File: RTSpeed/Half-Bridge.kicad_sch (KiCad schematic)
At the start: 8 parts, among them Q1 IRF1310, Q2 IRF1310, U1 IR2101

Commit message: Added STM32F411 development schematic
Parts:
- renumbered C2 to C1, C1 to C2, R2 to R1, R1 to R2
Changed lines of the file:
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@@
   (symbol (lib_id "power:GND") (at 48.26 79.375 0) (unit 1)
     (in_bom yes) (on_board yes) (dnp no)
-    (property "Reference" "#PWR03" (at 48.26 85.725 0)
+    (property "Reference" "#PWR02" (at 48.26 85.725 0)
       (effects (font (size 1.27 1.27)) hide)
     )
@@
     (instances
       (project "RTSpeed"
-        (path "/fc8dd9a9-f99a-4338-8182-2c8b4b8ed6dd"
-          (reference "#PWR03") (unit 1)
-        )
         (path "/fc8dd9a9-f99a-4338-8182-2c8b4b8ed6dd/b5458e57-2ddd-4d30-9620-d640c1a391c8"
           (reference "#PWR02") (unit 1)
@@
   (symbol (lib_id "Device:R_US") (at 85.09 95.885 90) (unit 1)
     (in_bom yes) (on_board yes) (dnp no)
-    (property "Reference" "R1" (at 85.09 90.805 90)
+    (property "Reference" "R2" (at 85.09 90.805 90)
       (effects (font (size 1.27 1.27)))
     )
@@
     (instances
       (project "RTSpeed"
-        (path "/fc8dd9a9-f99a-4338-8182-2c8b4b8ed6dd"
-          (reference "R1") (unit 1)
-        )
         (path "/fc8dd9a9-f99a-4338-8182-2c8b4b8ed6dd/b5458e57-2ddd-4d30-9620-d640c1a391c8"
           (reference "R2") (unit 1)
@@
     (instances
       (project "RTSpeed"
-        (path "/fc8dd9a9-f99a-4338-8182-2c8b4b8ed6dd"
-          (reference "Q1") (unit 1)
-        )
         (path "/fc8dd9a9-f99a-4338-8182-2c8b4b8ed6dd/b5458e57-2ddd-4d30-9620-d640c1a391c8"
           (reference "Q1") (unit 1)
@@
     (instances
       (project "RTSpeed"
-        (path "/fc8dd9a9-f99a-4338-8182-2c8b4b8ed6dd"
-          (reference "D1") (unit 1)
-        )
         (path "/fc8dd9a9-f99a-4338-8182-2c8b4b8ed6dd/b5458e57-2ddd-4d30-9620-d640c1a391c8"
           (reference "D1") (unit 1)
@@
     (instances
       (project "RTSpeed"
-        (path "/fc8dd9a9-f99a-4338-8182-2c8b4b8ed6dd"
+        (path "/fc8dd9a9-f99a-4338-8182-2c8b4b8ed6dd/b5458e57-2ddd-4d30-9620-d640c1a391c8"
           (reference "U1") (unit 1)
         )
-        (path "/fc8dd9a9-f99a-4338-8182-2c8b4b8ed6dd/b5458e57-2ddd-4d30-9620-d640c1a391c8"
-          (reference "U1") (unit 1)
-        )
         (path "/fc8dd9a9-f99a-4338-8182-2c8b4b8ed6dd/f8c306d8-017c-4a71-a4b7-a44622ec1e7a"
           (reference "U2") (unit 1)
@@
   (symbol (lib_id "power:GND") (at 96.52 100.965 0) (unit 1)
     (in_bom yes) (on_board yes) (dnp no)
-    (property "Reference" "#PWR02" (at 96.52 107.315 0)
+    (property "Reference" "#PWR04" (at 96.52 107.315 0)
       (effects (font (size 1.27 1.27)) hide)
     )
@@
     (instances
       (project "RTSpeed"
-        (path "/fc8dd9a9-f99a-4338-8182-2c8b4b8ed6dd"
-          (reference "#PWR02") (unit 1)
-        )
         (path "/fc8dd9a9-f99a-4338-8182-2c8b4b8ed6dd/b5458e57-2ddd-4d30-9620-d640c1a391c8"
           (reference "#PWR04") (unit 1)
@@
   (symbol (lib_id "Device:R_US") (at 85.09 83.185 90) (unit 1)
     (in_bom yes) (on_board yes) (dnp no)
-    (property "Reference" "R2" (at 85.09 78.105 90)
+    (property "Reference" "R1" (at 85.09 78.105 90)
       (effects (font (size 1.27 1.27)))
     )
@@
     (instances
       (project "RTSpeed"
-        (path "/fc8dd9a9-f99a-4338-8182-2c8b4b8ed6dd"
-          (reference "R2") (unit 1)
-        )
         (path "/fc8dd9a9-f99a-4338-8182-2c8b4b8ed6dd/b5458e57-2ddd-4d30-9620-d640c1a391c8"
           (reference "R1") (unit 1)
@@
   (symbol (lib_id "Device:C") (at 48.26 75.565 0) (unit 1)
     (in_bom yes) (on_board yes) (dnp no) (fields_autoplaced)
-    (property "Reference" "C2" (at 52.07 74.2949 0)
+    (property "Reference" "C1" (at 52.07 74.2949 0)
       (effects (font (size 1.27 1.27)) (justify left))
     )
@@
     (instances
       (project "RTSpeed"
-        (path "/fc8dd9a9-f99a-4338-8182-2c8b4b8ed6dd"
-          (reference "C2") (unit 1)
-        )
         (path "/fc8dd9a9-f99a-4338-8182-2c8b4b8ed6dd/b5458e57-2ddd-4d30-9620-d640c1a391c8"
           (reference "C1") (unit 1)
@@
     (instances
       (project "RTSpeed"
-        (path "/fc8dd9a9-f99a-4338-8182-2c8b4b8ed6dd"
+        (path "/fc8dd9a9-f99a-4338-8182-2c8b4b8ed6dd/b5458e57-2ddd-4d30-9620-d640c1a391c8"
           (reference "Q2") (unit 1)
         )
-        (path "/fc8dd9a9-f99a-4338-8182-2c8b4b8ed6dd/b5458e57-2ddd-4d30-9620-d640c1a391c8"
-          (reference "Q2") (unit 1)
-        )
         (path "/fc8dd9a9-f99a-4338-8182-2c8b4b8ed6dd/f8c306d8-017c-4a71-a4b7-a44622ec1e7a"
           (reference "Q4") (unit 1)
@@
   (symbol (lib_id "power:GND") (at 62.23 100.965 0) (unit 1)
     (in_bom yes) (on_board yes) (dnp no)
-    (property "Reference" "#PWR04" (at 62.23 107.315 0)
+    (property "Reference" "#PWR03" (at 62.23 107.315 0)
       (effects (font (size 1.27 1.27)) hide)
     )
@@
     (instances
       (project "RTSpeed"
-        (path "/fc8dd9a9-f99a-4338-8182-2c8b4b8ed6dd"
-          (reference "#PWR04") (unit 1)
-        )
         (path "/fc8dd9a9-f99a-4338-8182-2c8b4b8ed6dd/b5458e57-2ddd-4d30-9620-d640c1a391c8"
           (reference "#PWR03") (unit 1)
@@
   (symbol (lib_id "Device:C_Polarized_US") (at 73.025 88.265 0) (unit 1)
     (in_bom yes) (on_board yes) (dnp no)
-    (property "Reference" "C1" (at 76.2 86.995 0)
+    (property "Reference" "C2" (at 76.2 86.995 0)
       (effects (font (size 1.27 1.27)) (justify left))
     )
@@
     (instances
       (project "RTSpeed"
-        (path "/fc8dd9a9-f99a-4338-8182-2c8b4b8ed6dd"
-          (reference "C1") (unit 1)
-        )
         (path "/fc8dd9a9-f99a-4338-8182-2c8b4b8ed6dd/b5458e57-2ddd-4d30-9620-d640c1a391c8"
           (reference "C2") (unit 1)
@@
     (instances
       (project "RTSpeed"
-        (path "/fc8dd9a9-f99a-4338-8182-2c8b4b8ed6dd"
+        (path "/fc8dd9a9-f99a-4338-8182-2c8b4b8ed6dd/b5458e57-2ddd-4d30-9620-d640c1a391c8"
           (reference "#PWR01") (unit 1)
-        )
-        (path "/fc8dd9a9-f99a-4338-8182-2c8b4b8ed6dd/b5458e57-2ddd-4d30-9620-d640c1a391c8"
-          (reference "#PWR01") (unit 1)

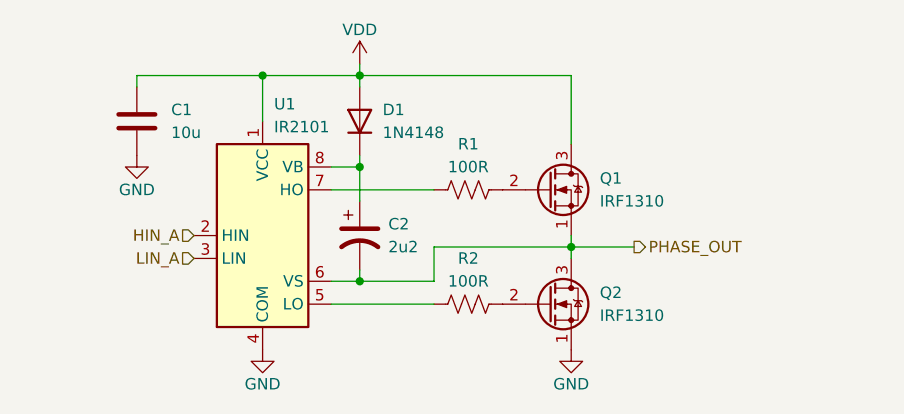
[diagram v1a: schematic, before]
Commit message: Connected Inverter
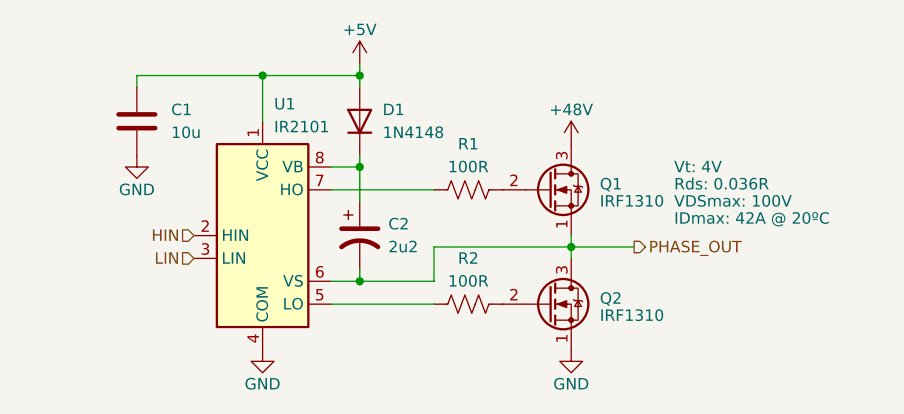
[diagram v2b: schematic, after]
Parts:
- Q1: IDmax (none) -> 42A @ 20ºC; Rds (none) -> 0.036R; VDSmax (none) -> 100V; Vt (none) -> 4V
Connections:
- net HIN_A renamed HIN
- net LIN_A renamed LIN
- net VDD renamed +5V
- net +5V: no longer Q1.3 (D)
- new net +48V: Q1.3 (D)
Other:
- title: (none) -> Half Bridge

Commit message: updated inverter model
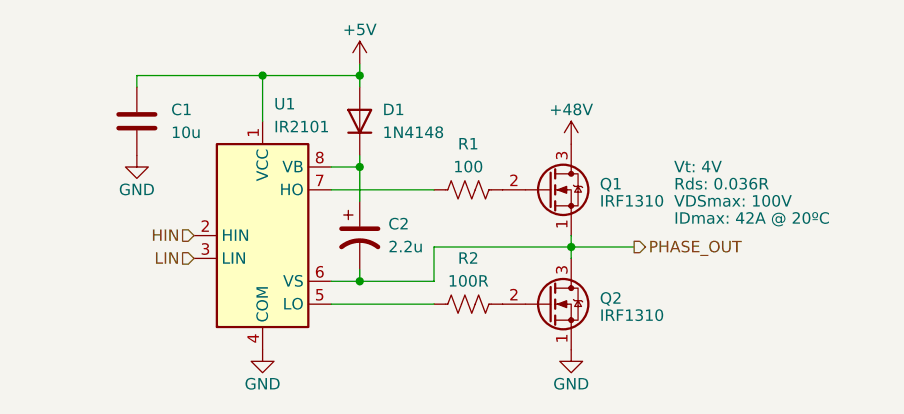
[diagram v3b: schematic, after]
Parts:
- C2: value 2u2 -> 2.2u
- R1: value 100R -> 100
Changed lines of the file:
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@@
       (effects (font (size 1.27 1.27)) (justify left))
+    )
+    (property "Sim.Library" "D:\\dev\\RTSpeed\\simulation\\models\\irf1310ns.spi" (at 93.98 83.185 0)
+      (effects (font (size 1.27 1.27)) hide)
+    )
+    (property "Sim.Name" "irf1310ns" (at 93.98 83.185 0)
+      (effects (font (size 1.27 1.27)) hide)
+    )
+    (property "Sim.Device" "SUBCKT" (at 93.98 83.185 0)
+      (effects (font (size 1.27 1.27)) hide)
+    )
+    (property "Sim.Pins" "1=1 2=2 3=3" (at 93.98 83.185 0)
+      (effects (font (size 1.27 1.27)) hide)
     )
     (pin "1")
@@
       (effects (font (size 1.27 1.27)) hide)
     )
-    (property "Sim.Device" "D" (at 73.025 75.565 0)
-      (effects (font (size 1.27 1.27)) hide)
-    )
-    (property "Sim.Pins" "1=K 2=A" (at 73.025 75.565 0)
+    (property "Sim.Device" "SUBCKT" (at 73.025 75.565 0)
+      (effects (font (size 1.27 1.27)) hide)
+    )
+    (property "Sim.Pins" "1=1 2=2" (at 73.025 75.565 0)
+      (effects (font (size 1.27 1.27)) hide)
+    )
+    (property "Sim.Library" "D:\\dev\\RTSpeed\\simulation\\models\\1N4148.lib" (at 73.025 75.565 0)
+      (effects (font (size 1.27 1.27)) hide)
+    )
+    (property "Sim.Name" "1N4148" (at 73.025 75.565 0)
       (effects (font (size 1.27 1.27)) hide)
     )
@@
     )
     (property "Datasheet" "https://www.infineon.com/dgdl/ir2101.pdf?fileId=5546d462533600a4015355c7a755166c" (at 62.23 88.265 0)
+      (effects (font (size 1.27 1.27)) hide)
+    )
+    (property "Sim.Library" "D:\\dev\\RTSpeed\\simulation\\models\\IR2101.lib" (at 62.23 88.265 0)
+      (effects (font (size 1.27 1.27)) hide)
+    )
+    (property "Sim.Name" "IR2101" (at 62.23 88.265 0)
+      (effects (font (size 1.27 1.27)) hide)
+    )
+    (property "Sim.Device" "SUBCKT" (at 62.23 88.265 0)
+      (effects (font (size 1.27 1.27)) hide)
+    )
+    (property "Sim.Pins" "1=VCC 2=HIN 3=LIN 4=COM 5=LO 6=VS 7=HO 8=VB" (at 62.23 88.265 0)
       (effects (font (size 1.27 1.27)) hide)
     )
@@
       (effects (font (size 1.27 1.27)))
     )
-    (property "Value" "100R" (at 85.09 80.645 90)
+    (property "Value" "100" (at 85.09 80.645 90)
       (effects (font (size 1.27 1.27)))
     )
@@
     )
     (property "Datasheet" "~" (at 85.09 83.185 0)
+      (effects (font (size 1.27 1.27)) hide)
+    )
+    (property "Sim.Device" "R" (at 85.09 83.185 0)
+      (effects (font (size 1.27 1.27)) hide)
+    )
+    (property "Sim.Pins" "1=+ 2=-" (at 85.09 83.185 0)
       (effects (font (size 1.27 1.27)) hide)
     )
@@
       (effects (font (size 1.27 1.27)) (justify left) hide)
     )
+    (property "Sim.Library" "D:\\dev\\RTSpeed\\simulation\\models\\irf1310ns.spi" (at 93.98 95.885 0)
+      (effects (font (size 1.27 1.27)) hide)
+    )
+    (property "Sim.Name" "irf1310ns" (at 93.98 95.885 0)
+      (effects (font (size 1.27 1.27)) hide)
+    )
+    (property "Sim.Device" "SUBCKT" (at 93.98 95.885 0)
+      (effects (font (size 1.27 1.27)) hide)
+    )
+    (property "Sim.Pins" "1=1 2=2 3=3" (at 93.98 95.885 0)
+      (effects (font (size 1.27 1.27)) hide)
+    )
     (pin "1")
     (pin "2")
@@
       (effects (font (size 1.27 1.27)) (justify left))
     )
-    (property "Value" "2u2" (at 76.2 89.535 0)
+    (property "Value" "2.2u" (at 76.2 89.535 0)
       (effects (font (size 1.27 1.27)) (justify left))
     )
@@
       (effects (font (size 1.27 1.27)) hide)
     )
+    (property "Sim.Device" "C" (at 73.025 88.265 0)
+      (effects (font (size 1.27 1.27)) hide)
+    )
+    (property "Sim.Pins" "1=+ 2=-" (at 73.025 88.265 0)
+      (effects (font (size 1.27 1.27)) hide)
+    )

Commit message: Added some footprints
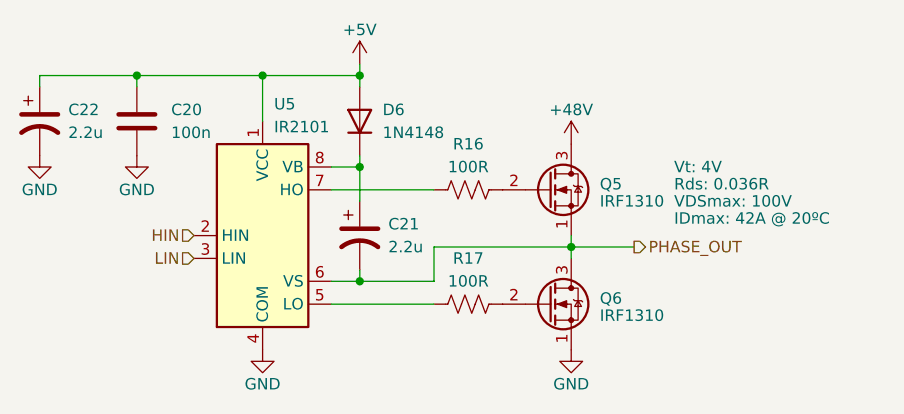
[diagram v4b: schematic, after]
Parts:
- added C22: 2.2u, Capacitor_THT:CP_Radial_D5.0mm_P2.00mm, symbol Device:C_Polarized_US
- C20: renamed from C1; value 10u -> 100n; footprint (none) -> Capacitor_SMD:C_0603_1608Metric
- C21: renamed from C2; footprint (none) -> Capacitor_THT:CP_Radial_D5.0mm_P2.00mm
- D6: renamed from D1; footprint (none) -> Diode_SMD:D_SOD-123
- R16: renamed from R1; value 100 -> 100R; footprint (none) -> Resistor_SMD:R_0805_2012Metric
- R17: renamed from R2; footprint (none) -> Resistor_SMD:R_0805_2012Metric
- U5: renamed from U1; footprint (none) -> Package_DIP:DIP-8_W10.16mm
- renumbered Q1 to Q5, Q2 to Q6
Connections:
- net +5V: now also C22.1
- net GND: now also C22.2
